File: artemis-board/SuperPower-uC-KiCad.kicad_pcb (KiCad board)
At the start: 4 copper layers, 45.1 x 45.1 mm, 88 parts, among them J1 Battery connector, J10 External NTC, J2 Thermistor, J3 USB_B_Micro, J4 Solar in, J7 unprotected BAT in, J8 regulator board, Q1 2N7002, Q10 AO3401A, Q2 2N7002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

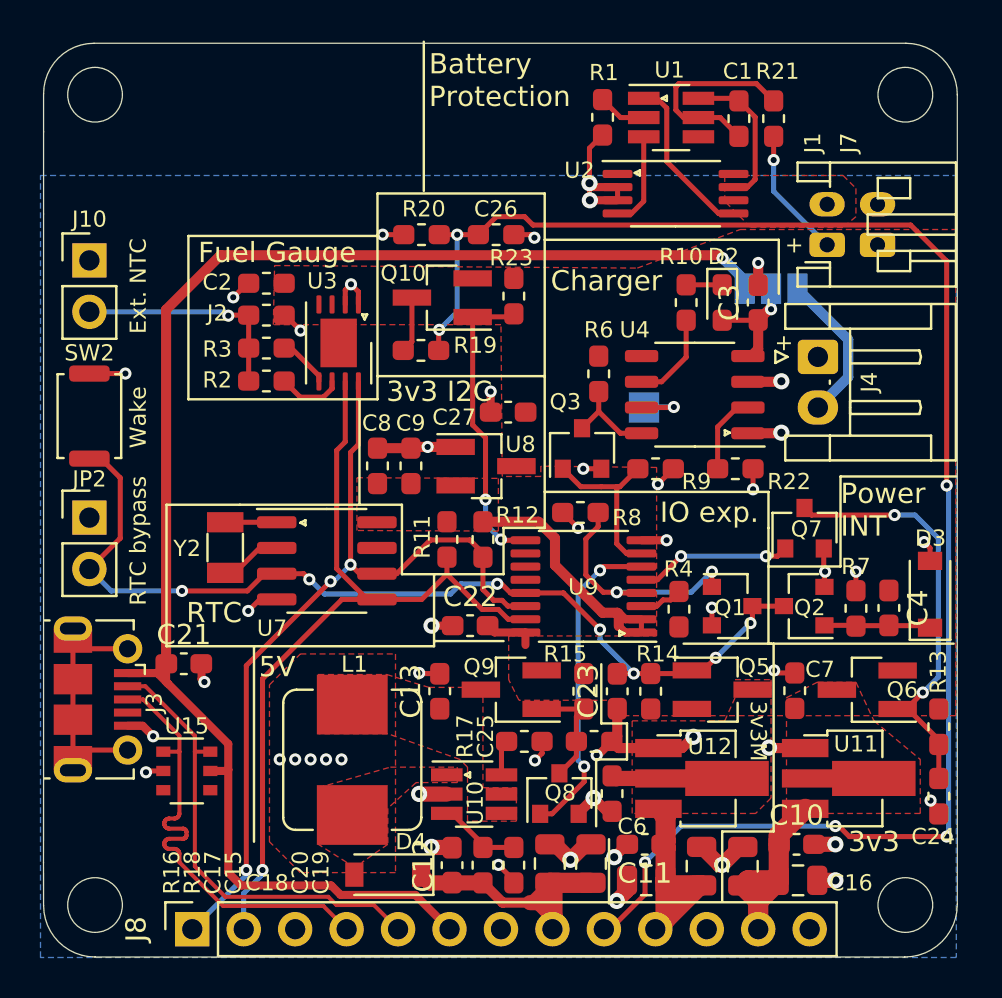
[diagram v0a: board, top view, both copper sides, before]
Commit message: added cap to Vbat rail for more stability
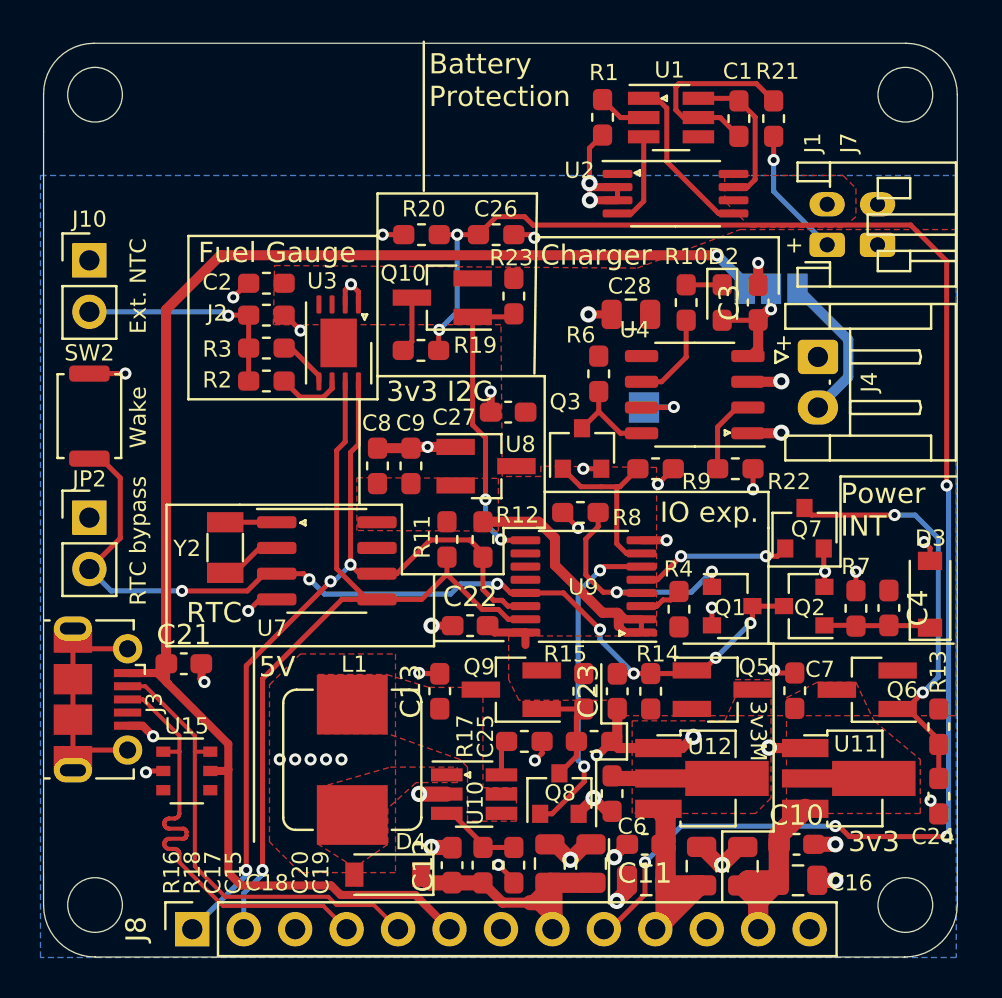
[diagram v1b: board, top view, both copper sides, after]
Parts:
- added C28: 22µF, Capacitor_SMD:C_0805_2012Metric, F.Cu at (162.2, 91.7)
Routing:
- net GND: track 69.4 -> 70.6 mm, vias 49 -> 50

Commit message: fixed silk being moved on some caps
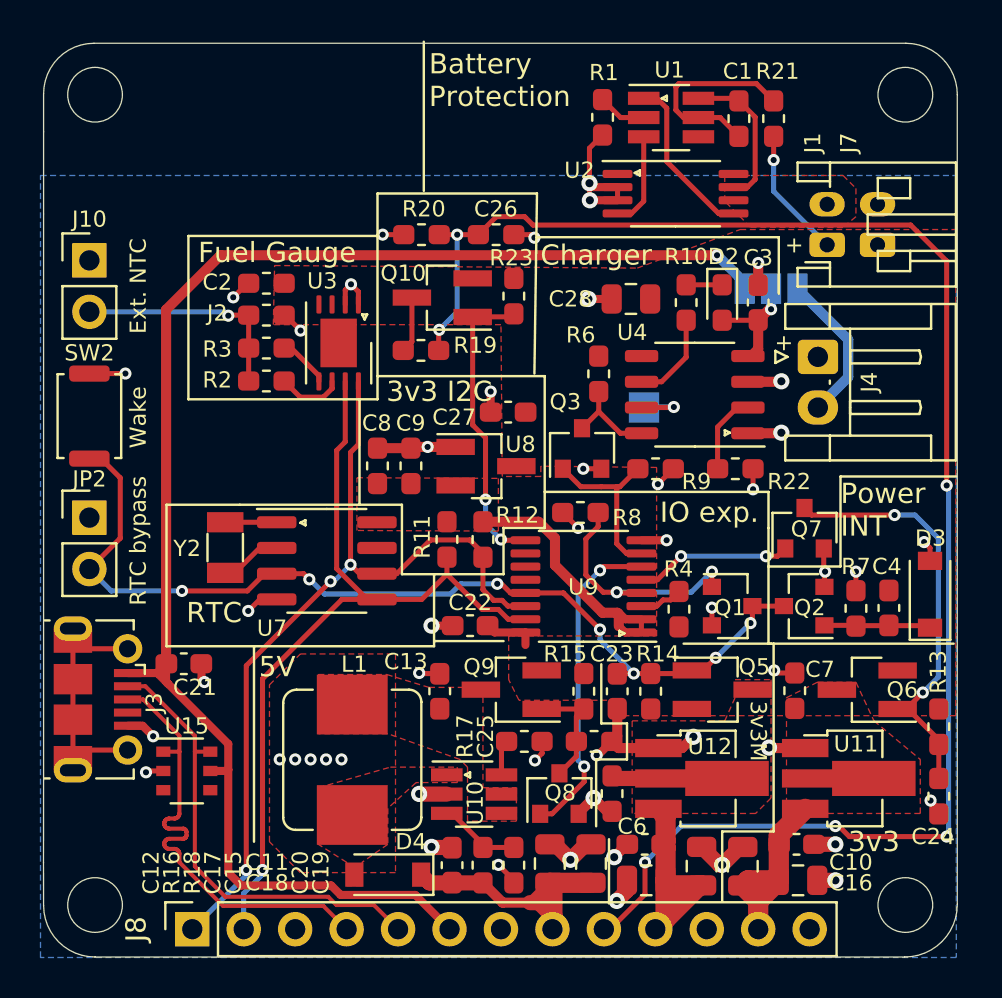
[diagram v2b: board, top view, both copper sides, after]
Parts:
- moved C28 0.76 mm to (162.2, 90.9)

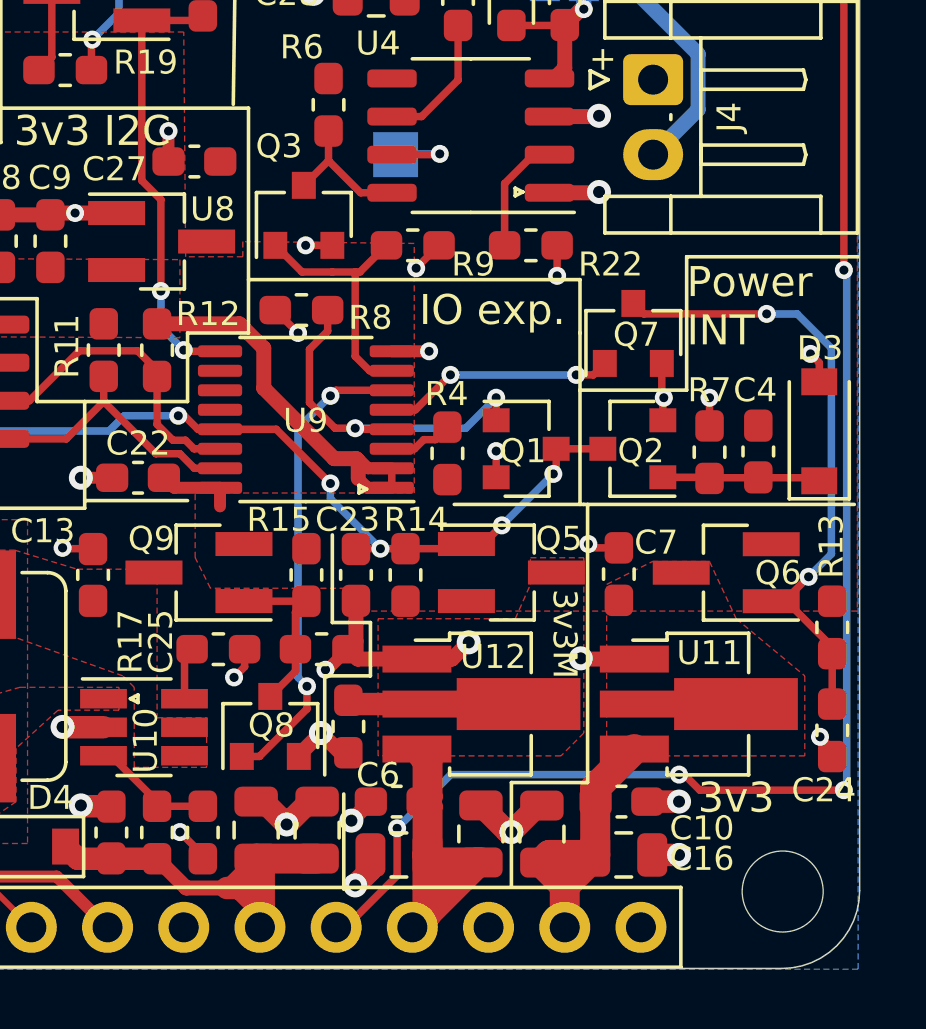
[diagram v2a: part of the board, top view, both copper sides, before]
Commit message: added jumpers for use without io expander
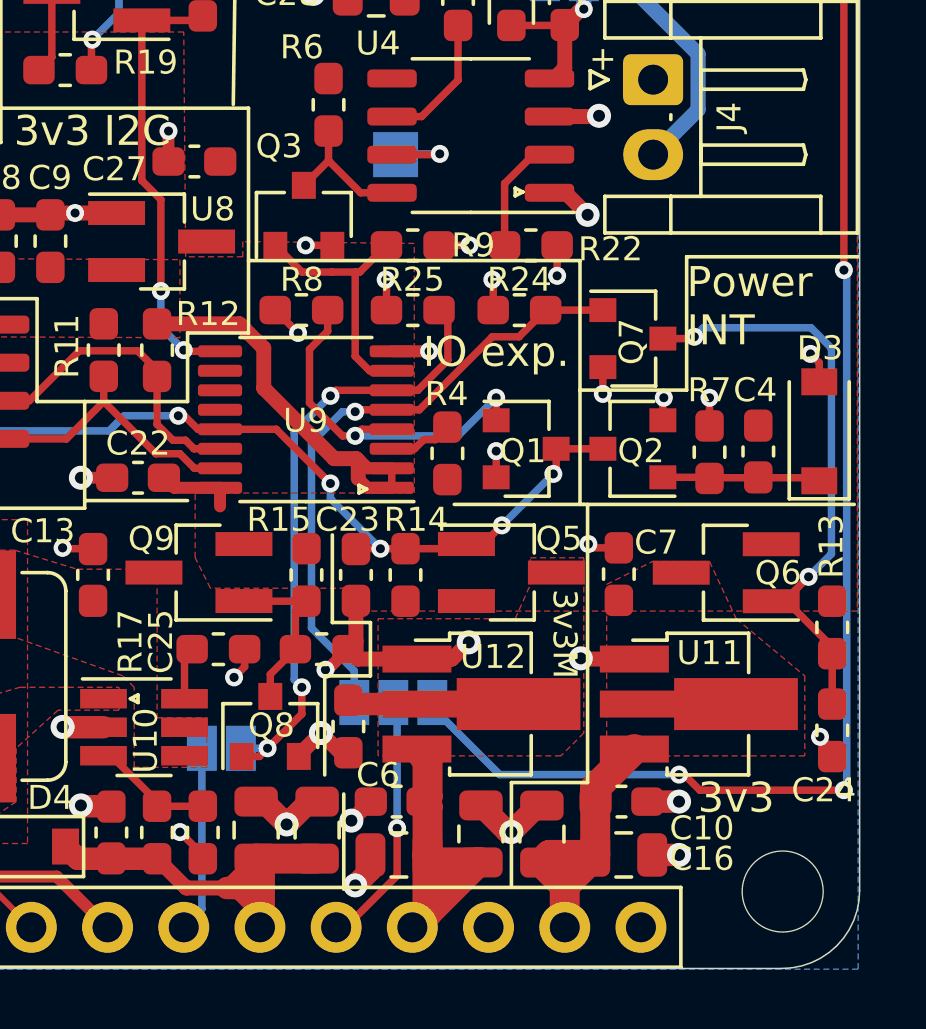
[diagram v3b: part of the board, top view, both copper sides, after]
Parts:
- added JP3: jumper, Jumper:SolderJumper-3_P1.3mm_Open_Pad1.0x1.5mm, B.Cu at (162.8, 114.6)
- added JP4: Jumper_NO_Small, Jumper:SolderJumper-2_P1.3mm_Open_Pad1.0x1.5mm, B.Cu at (157.1, 116.1)
- added R24: 1M, Resistor_SMD:R_0603_1608Metric_Pad1.05x0.95mm_HandSolder, F.Cu at (167.0, 101.5)
- added R25: 1M, Resistor_SMD:R_0603_1608Metric_Pad1.05x0.95mm_HandSolder, F.Cu at (163.4, 101.5)
- moved Q7 0.17 mm to (170.8, 102.4), turned to 0 degrees
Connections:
- J8 pad 9: /RTC and Cut-Off Module/Vmeasure -> Net-(J8-Pad9)
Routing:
- net /RTC and Cut-Off Module/3v3V_EN: track 7.74 -> 20.8 mm, vias 2 -> 1
- net Net-(J8-Pad9): track 0.00 -> 8.84 mm, vias 0 -> 1
- net Net-(J8-Pad7): track 0.00 -> 6.22 mm
- net /RTC and Cut-Off Module/Vmeasure: track 81.4 -> 75.9 mm, vias 6 -> 5
- net /RTC and Cut-Off Module/5V_EN: track 16.0 -> 20.9 mm, vias 2 -> 3
- net GND: track 70.6 -> 72.3 mm, vias 50 -> 53
- net Net-(C24-Pad1): track 21.3 -> 20.1 mm
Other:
- board text added: "3v3_EN"
- board text added: "3v3_M"
- board text added: "5V_EN"
- board text added: "Vbat/2"
- board text removed: "3v3_MCU"
- board text removed: "VBat/2"

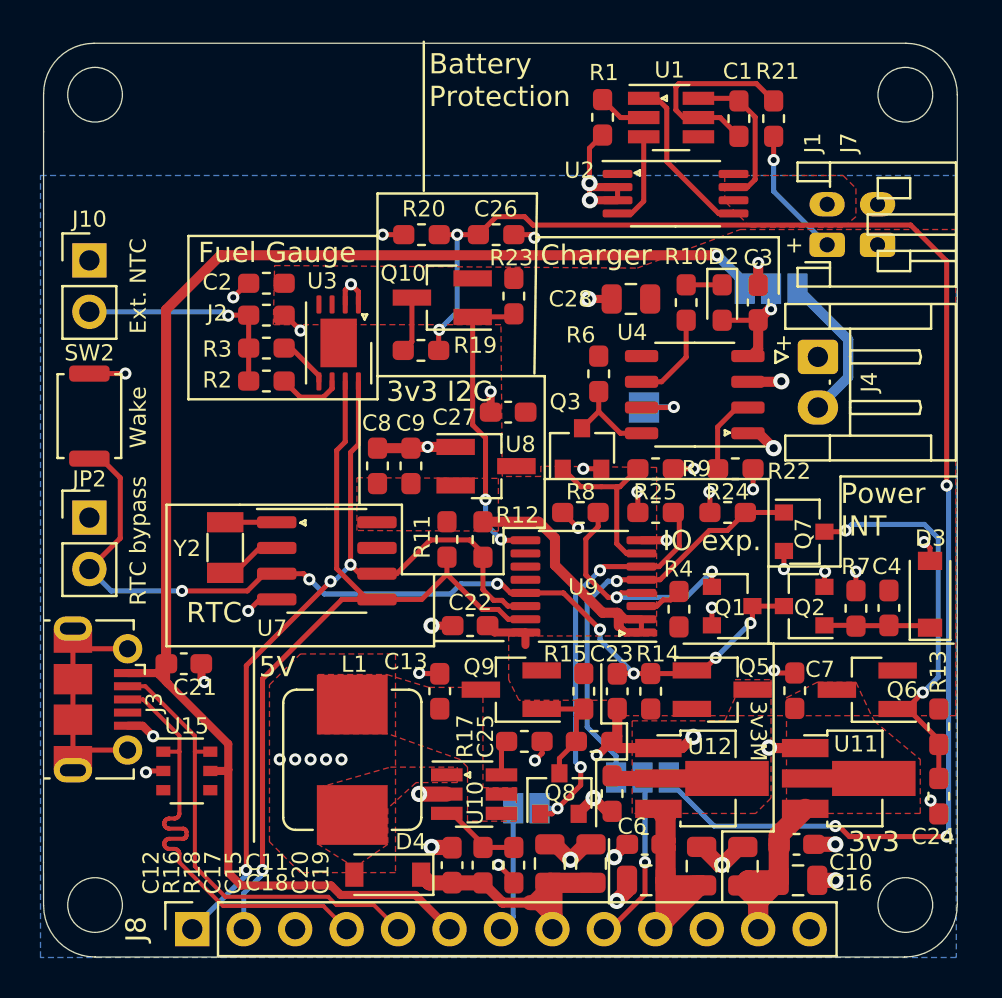
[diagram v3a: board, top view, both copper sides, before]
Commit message: connected VccP of io expander back to 3v3, changed some footprint
also added NMos so voltage divider can be used
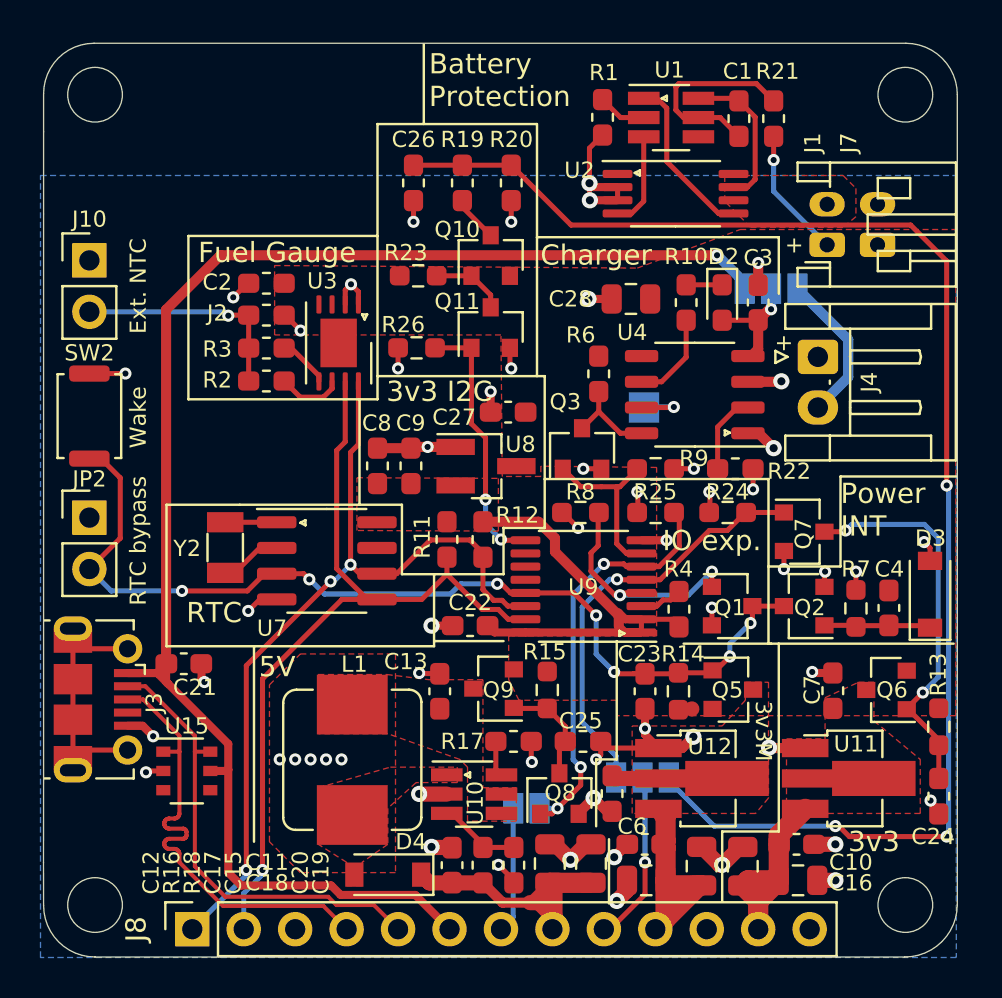
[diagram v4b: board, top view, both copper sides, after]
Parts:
- added Q11: 2N7002, Package_TO_SOT_SMD:SOT-23, F.Cu at (155.3, 92.3)
- added R26: 1M, Resistor_SMD:R_0603_1608Metric_Pad0.98x0.95mm_HandSolder, F.Cu at (151.6, 93.3)
- JP4: value Jumper_NO_Small -> Jumper 5v enable
- Q10, Q5, Q6, Q9: footprint Package_TO_SOT_SMD:SOT-23_Handsoldering -> Package_TO_SOT_SMD:SOT-23
- R13, R14, R15, R23, R24, R25, R7, R8, R9: footprint Resistor_SMD:R_0603_1608Metric_Pad1.05x0.95mm_HandSolder -> Resistor_SMD:R_0603_1608Metric_Pad0.98x0.95mm_HandSolder
- moved R19 8.52 mm to (153.9, 85.2), turned to 90 degrees
- moved R20 5.11 mm to (156.3, 85.2), turned to 270 degrees
- moved R23 4.83 mm to (151.7, 89.8), turned to 180 degrees
- moved C26 4.81 mm to (151.5, 85.2), turned to 90 degrees
- moved Q10 3.17 mm to (155.3, 88.8), turned to 90 degrees
- moved C7 1.88 mm to (172.2, 110.3)
- moved R15 1.80 mm to (158.1, 110.2)
- moved C23 1.37 mm to (162.9, 110.3)
- moved R14 1.37 mm to (164.6, 110.3)
- moved Q6 0.95 mm to (174.8, 110.2)
- moved Q9 0.87 mm to (155.4, 110.2)
- moved C25 0.55 mm to (159.9, 112.8)
- moved R17 0.53 mm to (156.4, 112.8)
- moved Q5 0.52 mm to (167.2, 110.2)
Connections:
- C22 pad 2: /Battery Module/VBAT -> /Charging Module/3v3_I2C
- R4 pad 1: /Battery Module/VBAT -> /Charging Module/3v3_I2C
- U9 pad 16: /Battery Module/VBAT -> /Charging Module/3v3_I2C
- U9 pad 9: Net-(Q10-Pad1) -> Net-(Q11-Pad1)
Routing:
- net Net-(Q11-Pad1): track 0.00 -> 13.2 mm, vias 0 -> 2
- net Net-(Q10-Pad1): track 15.5 -> 3.67 mm, vias 2 -> 0
- net /Charging Module/3v3_I2C: track 13.9 -> 24.2 mm
- net /RTC and Cut-Off Module/Vmeasure: track 75.9 -> 71.8 mm, vias 5 -> 3
- net /Battery Module/VBAT: track 9.99 -> 6.46 mm
- net GND: track 72.3 -> 75.2 mm, vias 53 -> 56
- net Net-(C24-Pad1): track 20.1 -> 19.2 mm
- net /RTC and Cut-Off Module/~INT: track 12.6 -> 11.8 mm

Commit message: removed unprotected connector, added jumper, moved cap to 3v3_mcu
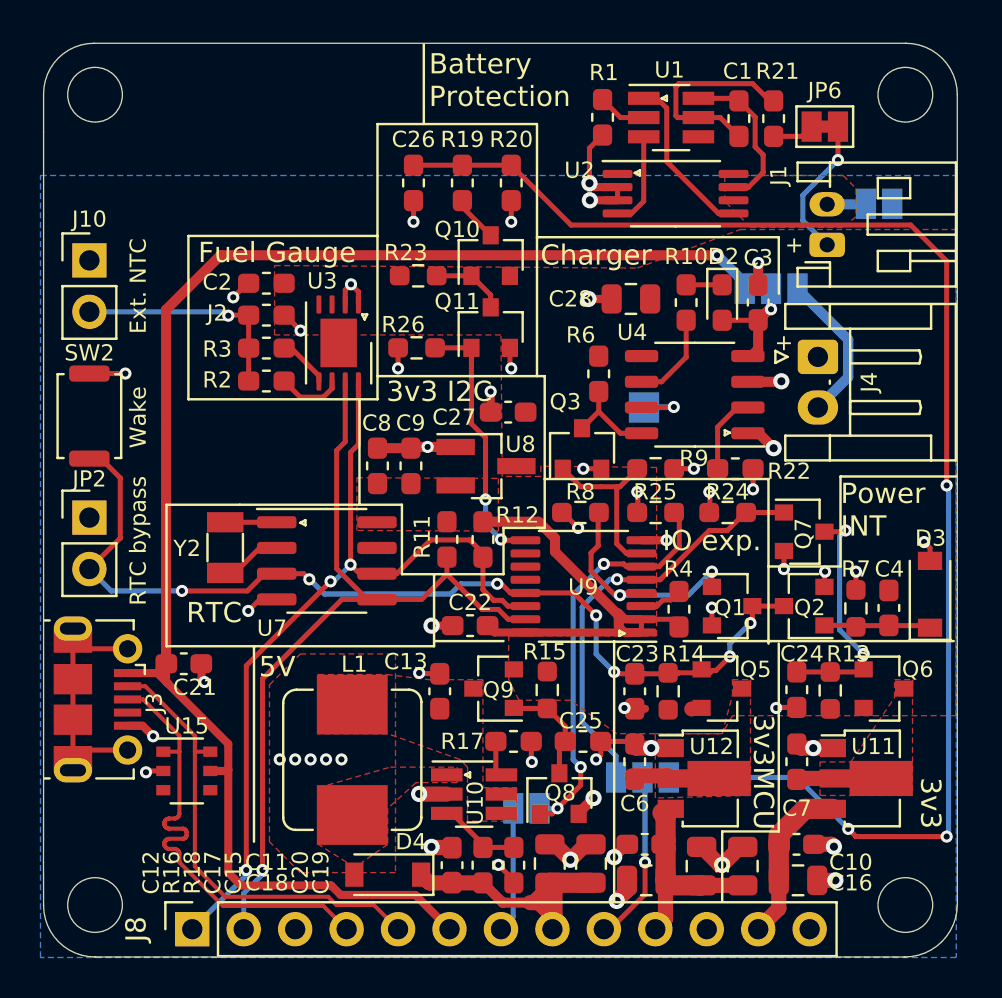
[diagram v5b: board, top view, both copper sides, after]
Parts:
- removed J7: unprotected BAT in, Connector_JST:JST_PH_S2B-PH-K_1x02_P2.00mm_Horizontal
- added JP5: Jumper_2_Open, Jumper:SolderJumper-2_P1.3mm_Open_Pad1.0x1.5mm, B.Cu at (174.5, 86.2)
- added JP6: Jumper_2_Bridged, Jumper:SolderJumper-2_P1.3mm_Bridged_Pad1.0x1.5mm, F.Cu at (171.8, 82.4)
- U11, U12: footprint Package_TO_SOT_SMD:SOT-89-3_Handsoldering -> Package_TO_SOT_SMD:SOT-89-3
- moved C24 8.76 mm to (170.4, 110.2)
- moved R13 5.65 mm to (172.1, 110.3), turned to 270 degrees
- moved C7 3.93 mm to (170.4, 113.8)
- moved C6 1.93 mm to (162.4, 113.8), turned to 90 degrees
- moved U11 0.86 mm to (173.8, 114.6)
- moved Q5 0.54 mm to (166.7, 110.2)
- moved C23 0.51 mm to (162.4, 110.3)
- moved R14 0.51 mm to (164.1, 110.3)
- moved Q6 0.14 mm to (174.7, 110.2), turned to 0 degrees
- moved U12 0.11 mm to (165.8, 114.6)
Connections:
- C19 pad 1: /3v3 -> /3v3_MCU
- R21 pad 1: /Battery Module/VBAT -> Net-(JP6-Pad2)
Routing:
- net Net-(C24-Pad1): track 19.2 -> 11.9 mm
- net GND: track 75.2 -> 70.5 mm, vias 56 -> 55
- net /Battery Module/BAT-: track 7.48 -> 9.77 mm
- net Net-(JP6-Pad2): track 0.00 -> 2.07 mm
- net /3v3: track 9.86 -> 8.27 mm
- net Net-(C7-Pad1): track 0.82 -> 1.89 mm
- net /3v3_MCU: track 11.4 -> 10.4 mm
- net /Battery Module/VBAT: track 6.46 -> 7.06 mm
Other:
- board text added: "3v3MCU"
- board text added: "v1.1 (2021-07)"
- board text removed: "3v3M"
- board text removed: "Battery in unprotected"
- board text removed: "v1.1 (2021-05)"
